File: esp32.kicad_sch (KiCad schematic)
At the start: 49 parts, among them J3 TC2030-IDC, J7 Conn_01x04, J8 ST7789 176x320, J8 USB_C_Receptacle_USB2.0, Q5 BSS123, SW1 EVQ-9P701P, U7 SN74AVC4T774, U9 ESP32-S3-WROOM-1, Y1 32.768kHz

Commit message: Fix some part numbers in the BOM
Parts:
- U9: DK 1965-ESP32-S3-WROOM-1-N16R8CT-ND -> 1965-ESP32-S3-WROOM-1U-N16R8CT-ND; PARTNO ESP32-S3-WROOM-1-N16R8 -> ESP32-S3-WROOM-1U-N16R8
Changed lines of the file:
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@@
       (effects (font (size 1.27 1.27)) hide)
     )
-    (property "DK" "1965-ESP32-S3-WROOM-1-N16R8CT-ND" (at 128.905 101.6 0)
+    (property "DK" "1965-ESP32-S3-WROOM-1U-N16R8CT-ND" (at 128.905 101.6 0)
       (effects (font (size 1.27 1.27)) hide)
     )
-    (property "PARTNO" "ESP32-S3-WROOM-1-N16R8" (at 128.905 101.6 0)
+    (property "PARTNO" "ESP32-S3-WROOM-1U-N16R8" (at 128.905 101.6 0)
       (effects (font (size 1.27 1.27)) hide)
     )

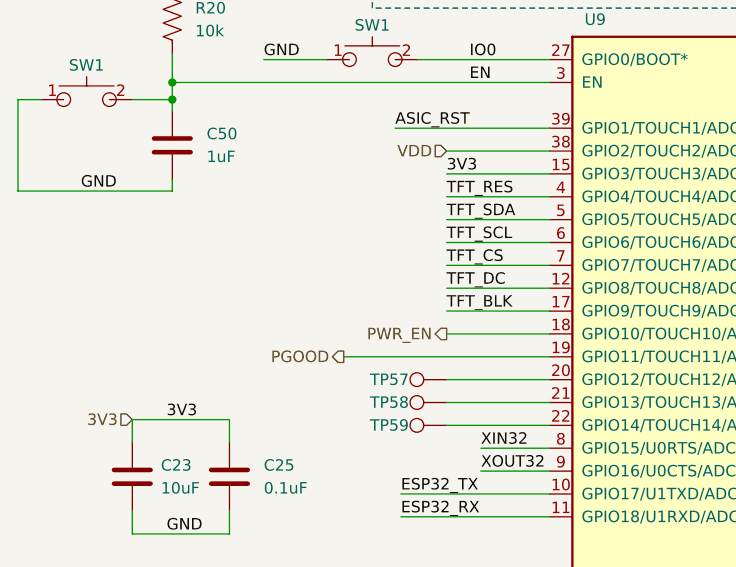
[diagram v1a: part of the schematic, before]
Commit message: fix mounting holes size/spacing, add pullup to PWR_EN signal
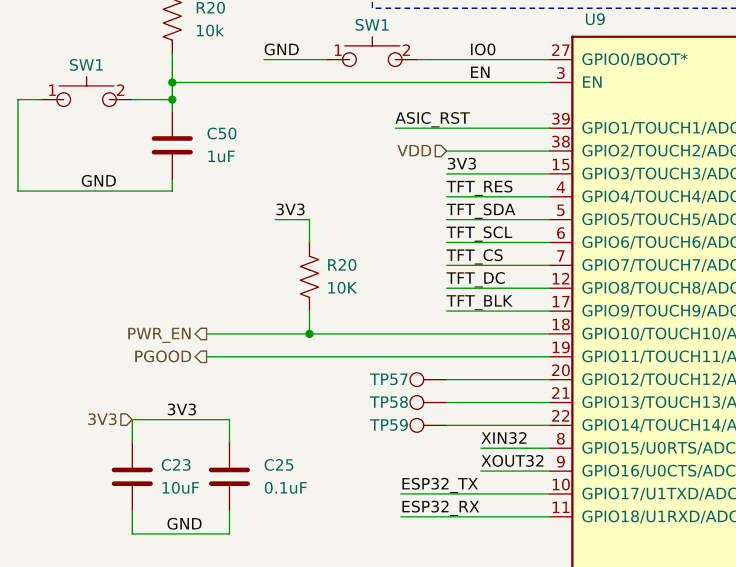
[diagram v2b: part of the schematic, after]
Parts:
- added R20: 10K, Resistor_SMD:R_0402_1005Metric, symbol Device:R_US
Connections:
- net 3V3: now also R20.1
- net PWR_EN: now also R20.2
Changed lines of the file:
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@@
   (junction (at 41.275 173.355) (diameter 0) (color 0 0 0 0)
+  )
+  (junction (at 46.355 101.6) (diameter 0) (color 0 0 0 0)
   )
   (junction (at 116.205 174.625) (diameter 0) (color 0 0 0 0)
@@
     (stroke (width 0) (type default))
   )
-  (wire (pts (xy 61.595 101.6) (xy 73.025 101.6))
+  (wire (pts (xy 34.925 101.6) (xy 46.355 101.6))
     (stroke (width 0) (type default))
   )
@@
     (stroke (width 0) (type default))
   )
+  (wire (pts (xy 46.355 101.6) (xy 73.025 101.6))
+    (stroke (width 0) (type default))
+  )
   (wire (pts (xy 224.155 128.905) (xy 224.155 125.73))
     (stroke (width 0) (type default))
@@
     (stroke (width 0) (type default))
   )
+  (wire (pts (xy 46.355 91.44) (xy 46.355 88.9))
+    (stroke (width 0) (type default))
+  )
   (wire (pts (xy 227.33 73.66) (xy 235.585 73.66))
     (stroke (width 0) (type default))
@@
     (stroke (width 0) (type default))
   )
-  (wire (pts (xy 50.165 104.14) (xy 73.025 104.14))
+  (wire (pts (xy 34.925 104.14) (xy 73.025 104.14))
     (stroke (width 0) (type default))
   )
@@
     (stroke (width 0) (type default))
   )
+  (wire (pts (xy 42.545 88.9) (xy 46.355 88.9))
+    (stroke (width 0) (type default))
+  )
   (wire (pts (xy 64.135 184.785) (xy 56.515 184.785))
     (stroke (width 0) (type default))
@@
   )
   (wire (pts (xy 235.585 71.12) (xy 227.33 71.12))
+    (stroke (width 0) (type default))
+  )
+  (wire (pts (xy 46.355 99.06) (xy 46.355 101.6))
     (stroke (width 0) (type default))
   )
@@
   )
   (label "TFT_SDA" (at 61.595 88.9 0) (fields_autoplaced)
+    (effects (font (size 1.27 1.27)) (justify left bottom))
+  )
+  (label "3V3" (at 42.545 88.9 0) (fields_autoplaced)
     (effects (font (size 1.27 1.27)) (justify left bottom))
   )
@@
     (effects (font (size 1.27 1.27)) (justify right))
   )
-  (hierarchical_label "PWR_EN" (shape output) (at 61.595 101.6 180) (fields_autoplaced)
+  (hierarchical_label "PWR_EN" (shape output) (at 34.925 101.6 180) (fields_autoplaced)
     (effects (font (size 1.27 1.27)) (justify right))
   )
@@
     (effects (font (size 1.27 1.27)) (justify right))
   )
-  (hierarchical_label "PGOOD" (shape output) (at 50.165 104.14 180) (fields_autoplaced)
+  (hierarchical_label "PGOOD" (shape output) (at 34.925 104.14 180) (fields_autoplaced)
     (effects (font (size 1.27 1.27)) (justify right))
   )
@@
         )
       )
+    )
+  )
+  (symbol (lib_id "Device:R_US") (at 46.355 95.25 0) (unit 1)
+    (in_bom yes) (on_board yes) (dnp no) (fields_autoplaced)
+    (property "Reference" "R20" (at 48.26 93.98 0)
+      (effects (font (size 1.27 1.27)) (justify left))
+    )
+    (property "Value" "10K" (at 48.26 96.52 0)
+      (effects (font (size 1.27 1.27)) (justify left))
+    )
+    (property "Footprint" "Resistor_SMD:R_0402_1005Metric" (at 47.371 95.504 90)
+      (effects (font (size 1.27 1.27)) hide)
+    )
+    (property "Datasheet" "~" (at 46.355 95.25 0)
+      (effects (font (size 1.27 1.27)) hide)
+    )
+    (property "DK" "311-10KJRCT-ND" (at 46.355 95.25 0)
+      (effects (font (size 1.27 1.27)) hide)
+    )
+    (property "PARTNO" "RC0402JR-0710KL" (at 46.355 95.25 0)
+      (effects (font (size 1.27 1.27)) hide)
+    )
+    (pin "1")
+    (pin "2")
+    (instances
+      (project "esp32"
+        (path "/dcd2fc1c-da48-40a9-b97c-5712d9530f4f"
+          (reference "R20") (unit 1)
+        )
+      )
+      (project "bitaxeHex"
+        (path "/e63e39d7-6ac0-4ffd-8aa3-1841a4541b55/ca857324-2ec8-447e-bd58-90d0c2e6b6d7"
+          (reference "R76") (unit 1)
+        )
+      )

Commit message: Start working on changelist for v301
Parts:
- added R20 (x2): 10K, Resistor_SMD:R_0402_1005Metric, symbol Device:R_US
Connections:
- net GND: now also R20.1
- net VDD: now also R20.1; no longer U9.38 (GPIO2/TOUCH2/ADC1_CH1)
- new net VDD_SAMPLE: R20.2, R20.2, U9.38 (GPIO2/TOUCH2/ADC1_CH1)
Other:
- moved on the sheet: C26, C50, J8, Q5, R20, R6, R7, SW1

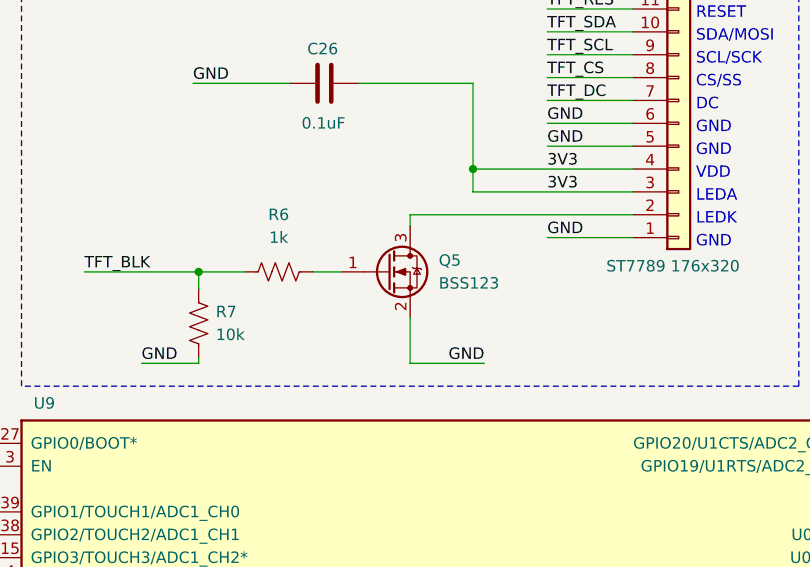
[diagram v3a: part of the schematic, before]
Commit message: finish schematic for power supply section, add part numbers and footprints
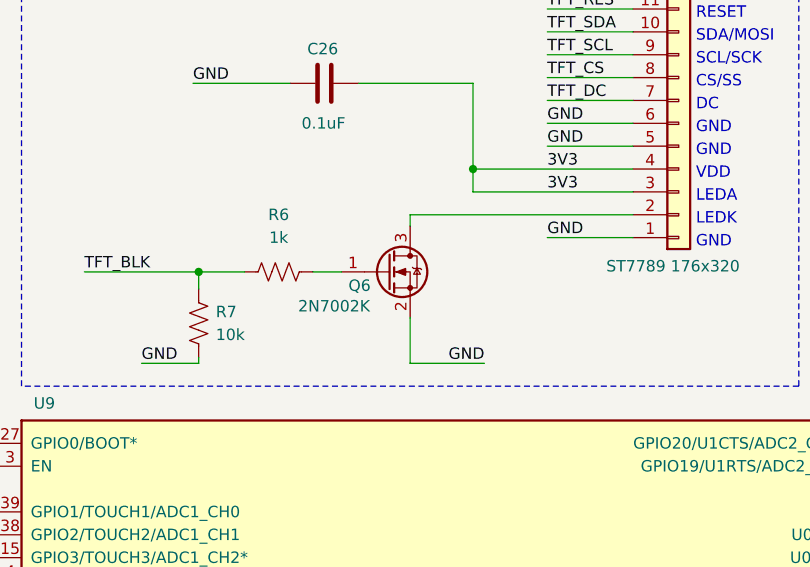
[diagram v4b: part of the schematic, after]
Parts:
- removed Q5: BSS123, Package_TO_SOT_SMD:SOT-23, symbol Device:Q_NMOS_GSD
- added Q6: 2N7002K, Package_TO_SOT_SMD:SOT-323_SC-70, symbol Transistor_FET:2N7002K
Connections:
- net GND: now also Q6.2 (S)
- net at R6.2: now also Q6.1 (G)
- net at J8.2 (Pin_2): now also Q6.3 (D)
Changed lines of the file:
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@@
-    )
-  )
-  (symbol (lib_id "Device:Q_NMOS_GSD") (at 116.205 52.07 0) (unit 1)
-    (in_bom yes) (on_board yes) (dnp no) (fields_autoplaced)
-    (property "Reference" "Q5" (at 121.92 50.8 0)
-      (effects (font (size 1.27 1.27)) (justify left))
-    )
-    (property "Value" "BSS123" (at 121.92 53.34 0)
-      (effects (font (size 1.27 1.27)) (justify left))
-    )
-    (property "Footprint" "Package_TO_SOT_SMD:SOT-23" (at 121.285 49.53 0)
-      (effects (font (size 1.27 1.27)) hide)
-    )
-    (property "Datasheet" "https://mm.digikey.com/Volume0/opasdata/d220001/medias/docus/4847/DS_4530_BSS123.pdf" (at 116.205 52.07 0)
-      (effects (font (size 1.27 1.27)) hide)
-    )
-    (property "DK" "4530-BSS123CT-ND" (at 116.205 52.07 0)
-      (effects (font (size 1.27 1.27)) hide)
-    )
-    (property "PARTNO" "BSS123" (at 116.205 52.07 0)
-      (effects (font (size 1.27 1.27)) hide)
-    )
-    (pin "1")
-    (pin "2")
-    (pin "3")
-    (instances
-      (project "bitaxeHex"
-        (path "/e63e39d7-6ac0-4ffd-8aa3-1841a4541b55/ca857324-2ec8-447e-bd58-90d0c2e6b6d7"
-          (reference "Q5") (unit 1)
-        )
-      )
     )
   )
@@
         )
       )
+    )
+  )
+  (symbol (lib_id "Transistor_FET:2N7002K") (at 116.205 52.07 0) (unit 1)
+    (in_bom yes) (on_board yes) (dnp no)
+    (property "Reference" "Q6" (at 111.887 53.594 0)
+      (effects (font (size 1.27 1.27)) (justify left))
+    )
+    (property "Value" "2N7002K" (at 106.299 55.88 0)
+      (effects (font (size 1.27 1.27)) (justify left))
+    )
+    (property "Footprint" "Package_TO_SOT_SMD:SOT-323_SC-70" (at 121.285 53.975 0)
+      (effects (font (size 1.27 1.27) italic) (justify left) hide)
+    )
+    (property "Datasheet" "https://www.diodes.com/assets/Datasheets/ds30896.pdf" (at 116.205 52.07 0)
+      (effects (font (size 1.27 1.27)) (justify left) hide)
+    )
+    (property "DK" "2N7002KWCT-ND" (at 116.205 52.07 0)
+      (effects (font (size 1.27 1.27)) hide)
+    )
+    (property "PARTNO" "2N7002KW" (at 116.205 52.07 0)
+      (effects (font (size 1.27 1.27)) hide)
+    )
+    (pin "1")
+    (pin "2")
+    (pin "3")
+    (instances
+      (project "bitaxeHex"
+        (path "/e63e39d7-6ac0-4ffd-8aa3-1841a4541b55/8ec0a9c6-2b78-44ef-a83d-9047d2828409"
+          (reference "Q6") (unit 1)
+        )
+        (path "/e63e39d7-6ac0-4ffd-8aa3-1841a4541b55/ca857324-2ec8-447e-bd58-90d0c2e6b6d7"
+          (reference "Q5") (unit 1)
+        )
+      )

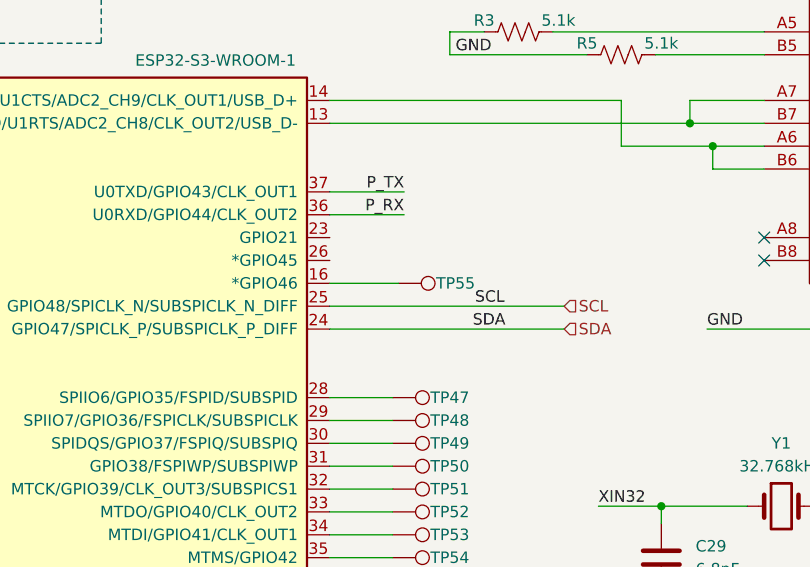
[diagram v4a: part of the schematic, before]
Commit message: More routing is done
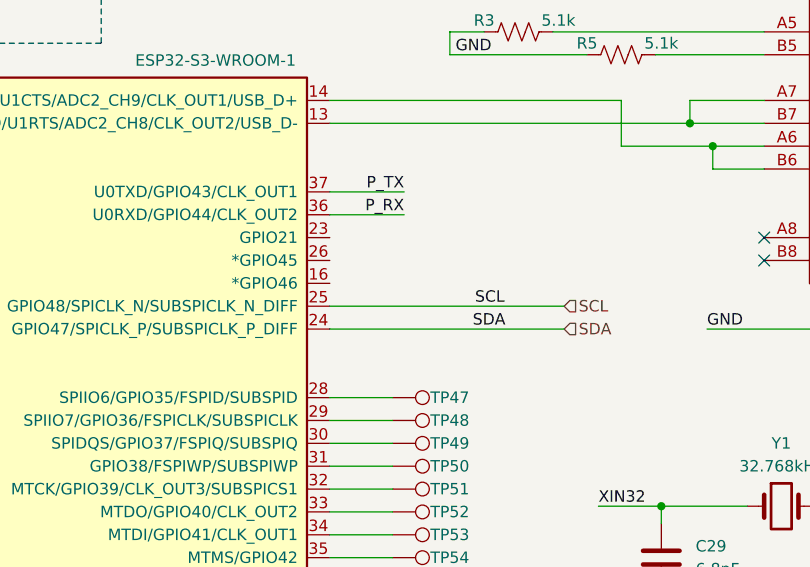
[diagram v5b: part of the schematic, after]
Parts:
- removed TP55: TestPoint, TestPoint:TestPoint_Pad_D1.0mm, symbol Connector:TestPoint
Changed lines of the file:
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@@
-    (stroke (width 0) (type default))
-  )
-  (wire (pts (xy 187.325 91.44) (xy 194.945 91.44))
     (stroke (width 0) (type default))
   )
@@
         )
       )
-    )
-  )
-  (symbol (lib_id "Connector:TestPoint") (at 194.945 91.44 270) (mirror x) (unit 1)
-    (in_bom no) (on_board yes) (dnp no)
-    (property "Reference" "TP55" (at 201.295 91.44 90)
-      (effects (font (size 1.27 1.27)))
-    )
-    (property "Value" "TestPoint" (at 200.66 90.1701 90)
-      (effects (font (size 1.27 1.27)) (justify left) hide)
-    )
-    (property "Footprint" "TestPoint:TestPoint_Pad_D1.0mm" (at 194.945 86.36 0)
-      (effects (font (size 1.27 1.27)) hide)
-    )
-    (property "Datasheet" "~" (at 194.945 86.36 0)
-      (effects (font (size 1.27 1.27)) hide)
-    )
-    (pin "1")
-    (instances
-      (project "bitaxeHex"
-        (path "/e63e39d7-6ac0-4ffd-8aa3-1841a4541b55/ca857324-2ec8-447e-bd58-90d0c2e6b6d7"
-          (reference "TP55") (unit 1)
-        )
-      )

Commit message: BOM cleanup
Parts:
- C23: DK 1276-1096-1-ND -> 490-18664-1-ND; PARTNO CL21A106KOQNNNE -> GRM21BR61H106ME43L
- C25, C26: DK 1292-1639-1-ND -> 478-KGM05AR71C104KHCT-ND; PARTNO 0402X104K100CT -> KGM05AR71C104KH
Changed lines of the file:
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@@
       (effects (font (size 1.778 1.5113)) (justify left bottom) hide)
     )
-    (property "DK" "1292-1639-1-ND" (at 116.205 167.005 0)
-      (effects (font (size 1.27 1.27)) hide)
-    )
-    (property "PARTNO" "0402X104K100CT" (at 116.205 167.005 0)
+    (property "DK" "478-KGM05AR71C104KHCT-ND" (at 116.205 167.005 0)
+      (effects (font (size 1.27 1.27)) hide)
+    )
+    (property "PARTNO" "KGM05AR71C104KH" (at 116.205 167.005 0)
       (effects (font (size 1.27 1.27)) hide)
     )
@@
       (effects (font (size 1.27 1.27)) hide)
     )
-    (property "DK" "1292-1639-1-ND" (at 109.22 31.115 0)
-      (effects (font (size 1.27 1.27)) hide)
-    )
-    (property "PARTNO" "0402X104K100CT" (at 109.22 31.115 0)
+    (property "DK" "478-KGM05AR71C104KHCT-ND" (at 109.22 31.115 0)
+      (effects (font (size 1.27 1.27)) hide)
+    )
+    (property "PARTNO" "KGM05AR71C104KH" (at 109.22 31.115 0)
       (effects (font (size 1.27 1.27)) hide)
     )
@@
       (effects (font (size 1.778 1.5113)) (justify left bottom) hide)
     )
-    (property "DK" "1292-1639-1-ND" (at 48.26 149.86 0)
-      (effects (font (size 1.27 1.27)) hide)
-    )
-    (property "PARTNO" "0402X104K100CT" (at 48.26 149.86 0)
+    (property "DK" "478-KGM05AR71C104KHCT-ND" (at 48.26 149.86 0)
+      (effects (font (size 1.27 1.27)) hide)
+    )
+    (property "PARTNO" "KGM05AR71C104KH" (at 48.26 149.86 0)
       (effects (font (size 1.27 1.27)) hide)
     )
@@
       (effects (font (size 1.27 1.27)) hide)
     )
-    (property "DK" "1292-1639-1-ND" (at 37.465 117.475 0)
-      (effects (font (size 1.27 1.27)) hide)
-    )
-    (property "PARTNO" "0402X104K100CT" (at 37.465 117.475 0)
+    (property "DK" "478-KGM05AR71C104KHCT-ND" (at 37.465 117.475 0)
+      (effects (font (size 1.27 1.27)) hide)
+    )
+    (property "PARTNO" "KGM05AR71C104KH" (at 37.465 117.475 0)
       (effects (font (size 1.27 1.27)) hide)
     )
@@
       (effects (font (size 1.27 1.27)) hide)
     )
-    (property "DK" "1276-1096-1-ND" (at 26.67 117.475 0)
-      (effects (font (size 1.27 1.27)) hide)
-    )
-    (property "PARTNO" "CL21A106KOQNNNE" (at 26.67 117.475 0)
-      (effects (font (size 1.27 1.27)) hide)
-    )
+    (property "DK" "490-18664-1-ND" (at 26.67 117.475 0)
+      (effects (font (size 1.27 1.27)) hide)
+    )
+    (property "PARTNO" "GRM21BR61H106ME43L" (at 26.67 117.475 0)
+      (effects (font (size 1.27 1.27)) hide)
+    )

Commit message: small schematic cleanup
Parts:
- R20: value 10K -> 10k
- R8: value 20K -> 20k
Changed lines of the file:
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@@
       (effects (font (size 1.27 1.27)))
     )
-    (property "Value" "10K" (at 34.29 82.55 90)
+    (property "Value" "10k" (at 34.29 82.55 90)
       (effects (font (size 1.27 1.27)))
     )
@@
       (effects (font (size 1.27 1.27)))
     )
-    (property "Value" "10K" (at 34.29 74.93 90)
+    (property "Value" "10k" (at 34.29 74.93 90)
       (effects (font (size 1.27 1.27)))
     )
@@
       (effects (font (size 1.27 1.27)) (justify left))
     )
-    (property "Value" "10K" (at 48.26 96.52 0)
+    (property "Value" "10k" (at 48.26 96.52 0)
       (effects (font (size 1.27 1.27)) (justify left))
     )
@@
       (effects (font (size 1.27 1.27)))
     )
-    (property "Value" "20K" (at 52.07 180.975 0)
-      (effects (font (size 1.27 1.27)))
-    )
+    (property "Value" "20k" (at 52.07 180.975 0)
+      (effects (font (size 1.27 1.27)))
+    )

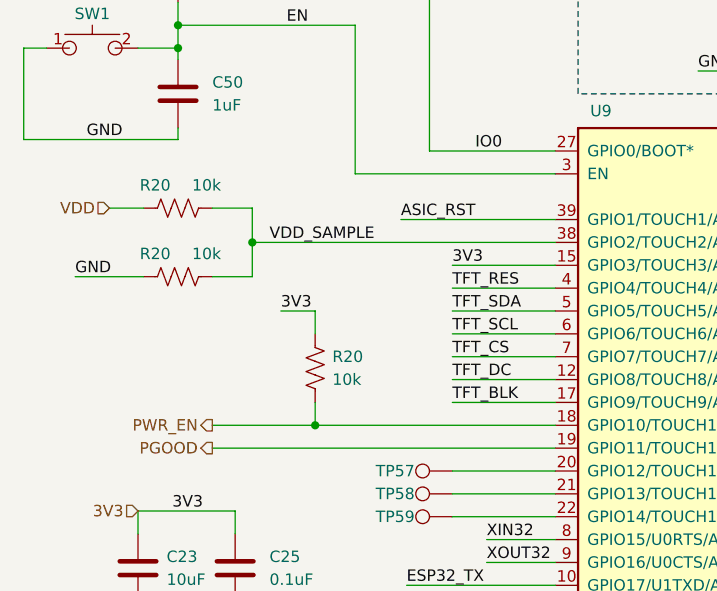
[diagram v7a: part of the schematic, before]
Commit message: update resistor values for VDD sample divider on schematic and BOM
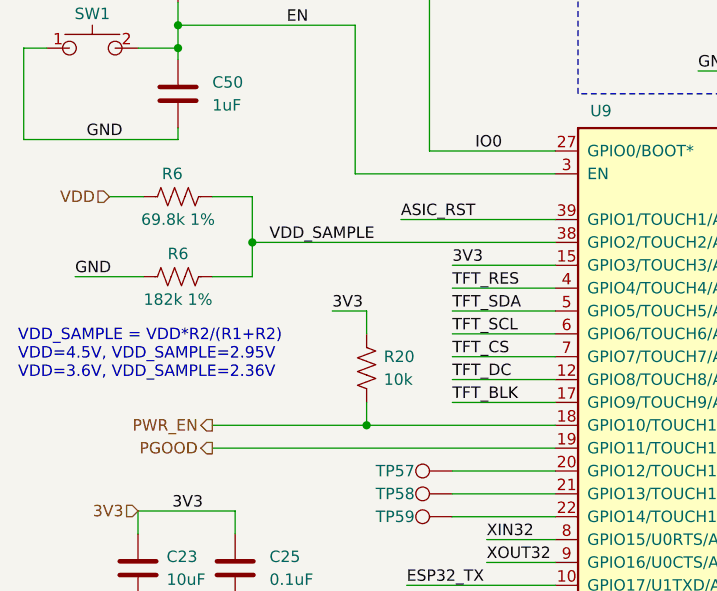
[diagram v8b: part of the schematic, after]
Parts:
- removed R20 (x3): 10k, Resistor_SMD:R_0402_1005Metric, symbol Device:R_US
- added R20: 10k, Resistor_SMD:R_0402_1005Metric, symbol Device:R_US
- added R6: 69.8k 1%, Resistor_SMD:R_0402_1005Metric, symbol Device:R_US
- added R6: 182k 1%, Resistor_SMD:R_0402_1005Metric, symbol Device:R_US
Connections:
- net 3V3: now also R20.1
- net GND: now also R6.2
- net PWR_EN: now also R20.2
- net VDD: now also R6.2
- net VDD_SAMPLE: now also R6.1, R6.1
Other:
- note added: "VDD_SAMPLE = VDD*R2/(R1+R2) VDD=4.5V, VDD_SAMPLE=2.95V VDD=3.6V, VDD_SAMPLE=2.36V"
